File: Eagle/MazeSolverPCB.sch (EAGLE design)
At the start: 26 parts, among them X1 TSW-113-02-S-S, X2 TSW-116-02-S-S, X3 TSW-113-02-S-S, X4 TSW-103-02-S-S, X5 TSW-103-02-S-S, X6 TSW-103-02-S-S, X7 TSW-103-02-S-S

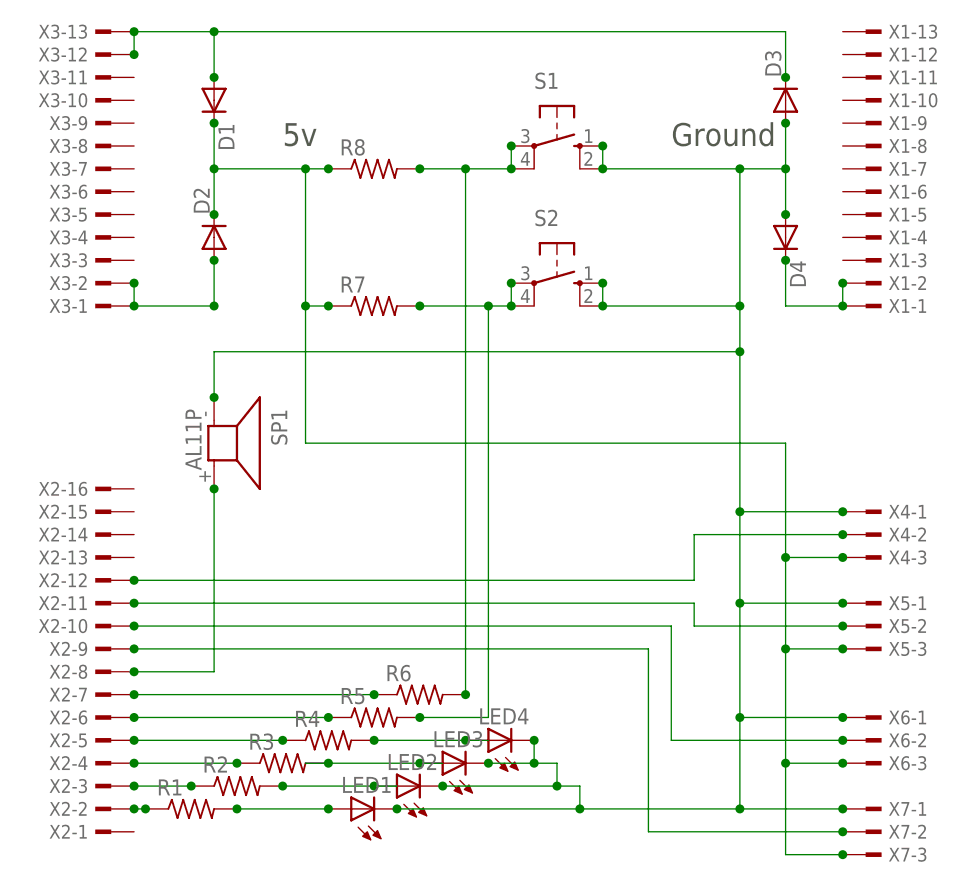
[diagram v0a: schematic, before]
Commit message: Fixed Resistor values and folder names
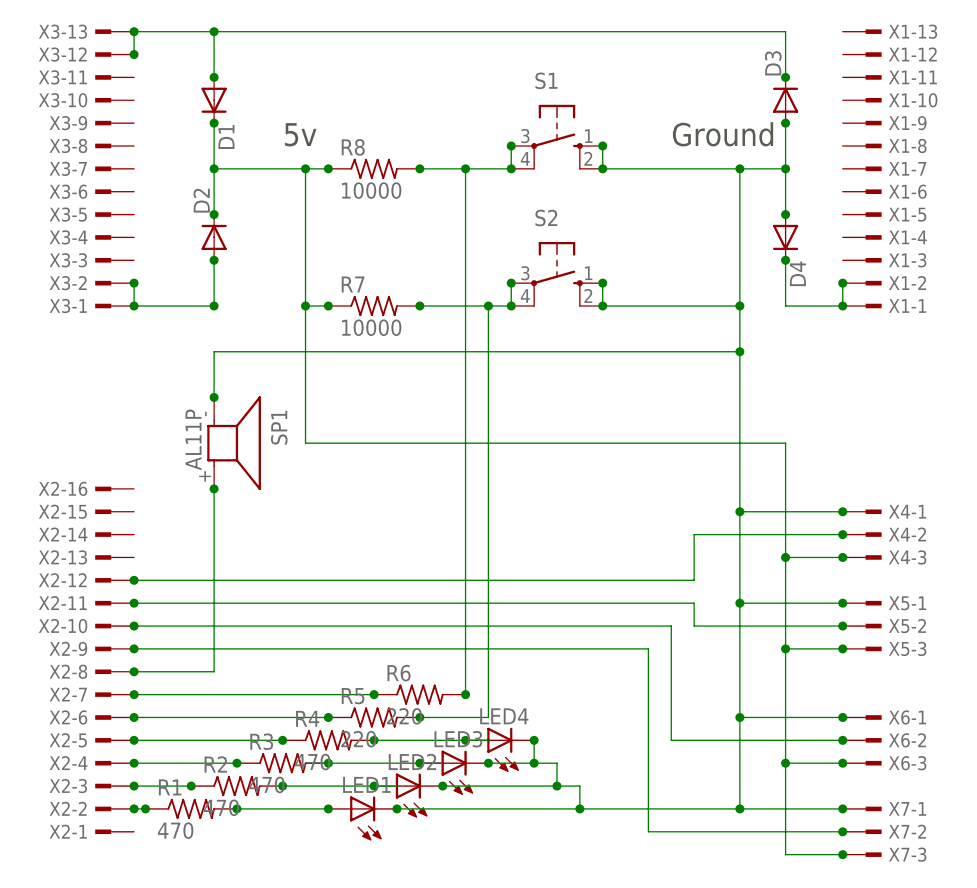
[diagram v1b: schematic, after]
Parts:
- R1, R2, R3, R4: value (none) -> 470
- R5, R6: value (none) -> 220
- R7, R8: value (none) -> 10000
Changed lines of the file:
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@@
 <setting verticaltext="up"/>
 </settings>
-<grid distance="0.05" unitdist="inch" unit="inch" style="lines" multiple="1" display="yes" altdistance="0.01" altunitdist="inch" altunit="inch"/>
+<grid distance="0.1" unitdist="inch" unit="inch" style="lines" multiple="1" display="no" altdistance="0.01" altunitdist="inch" altunit="inch"/>
 <layers>
 <layer number="1" name="Top" color="4" fill="1" visible="no" active="no"/>
@@
 </classes>
 <parts>
-<part name="R8" library="resistor" deviceset="R-US_" device="0207/7"/>
-<part name="R6" library="resistor" deviceset="R-US_" device="0207/7"/>
-<part name="R5" library="resistor" deviceset="R-US_" device="0207/7"/>
-<part name="R1" library="resistor" deviceset="R-US_" device="0207/7"/>
+<part name="R8" library="resistor" deviceset="R-US_" device="0207/7" value="10000"/>
+<part name="R6" library="resistor" deviceset="R-US_" device="0207/7" value="220"/>
+<part name="R5" library="resistor" deviceset="R-US_" device="0207/7" value="220"/>
+<part name="R1" library="resistor" deviceset="R-US_" device="0207/7" value="470"/>
 <part name="LED1" library="led" deviceset="TLLG4400" device="" value=""/>
 <part name="SP1" library="ajjeffers" deviceset="AL11P" device="" value="AL11P"/>
@@
 <part name="D3" library="aaron" deviceset="1N4004" device="" value=""/>
 <part name="D4" library="aaron" deviceset="1N4004" device="" value=""/>
-<part name="R7" library="resistor" deviceset="R-US_" device="0207/7"/>
-<part name="R2" library="resistor" deviceset="R-US_" device="0207/7"/>
-<part name="R3" library="resistor" deviceset="R-US_" device="0207/7"/>
-<part name="R4" library="resistor" deviceset="R-US_" device="0207/7"/>
+<part name="R7" library="resistor" deviceset="R-US_" device="0207/7" value="10000"/>
+<part name="R2" library="resistor" deviceset="R-US_" device="0207/7" value="470"/>
+<part name="R3" library="resistor" deviceset="R-US_" device="0207/7" value="470"/>
+<part name="R4" library="resistor" deviceset="R-US_" device="0207/7" value="470"/>
 <part name="LED2" library="led" deviceset="TLLG4400" device="" value=""/>
 <part name="LED3" library="led" deviceset="TLLG4400" device="" value=""/>
